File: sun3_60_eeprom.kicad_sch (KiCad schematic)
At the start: 19 parts, among them U2001 PAL16L8, U300 27512, U301 28C16, U302 7170, U303 32768Hz, U304 ALS273, U305 ALS373, U307 PAL20L8, U309 3-VOLT, U310 PAL20L8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

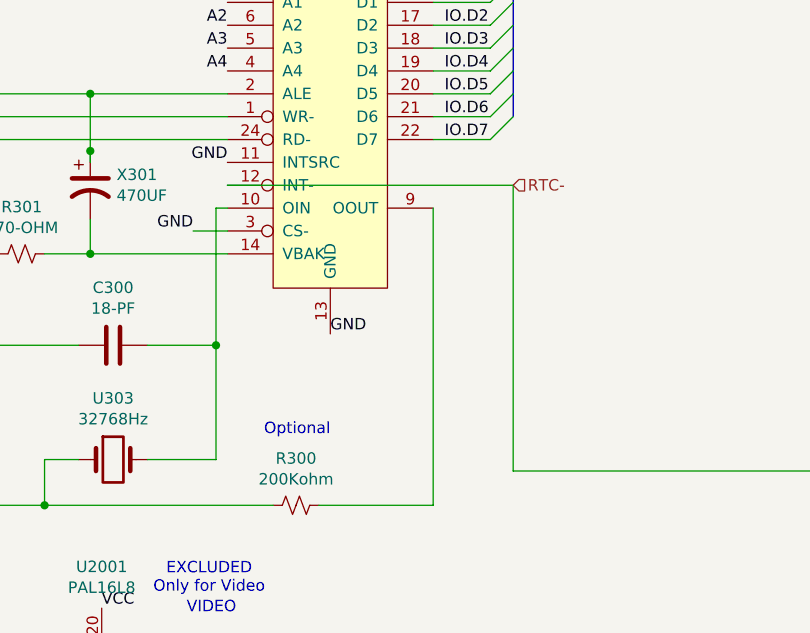
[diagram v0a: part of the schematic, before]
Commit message: Clean up before reorganizing the folders. The schematics and PCB reflect the fixes discovered during the prototype build.
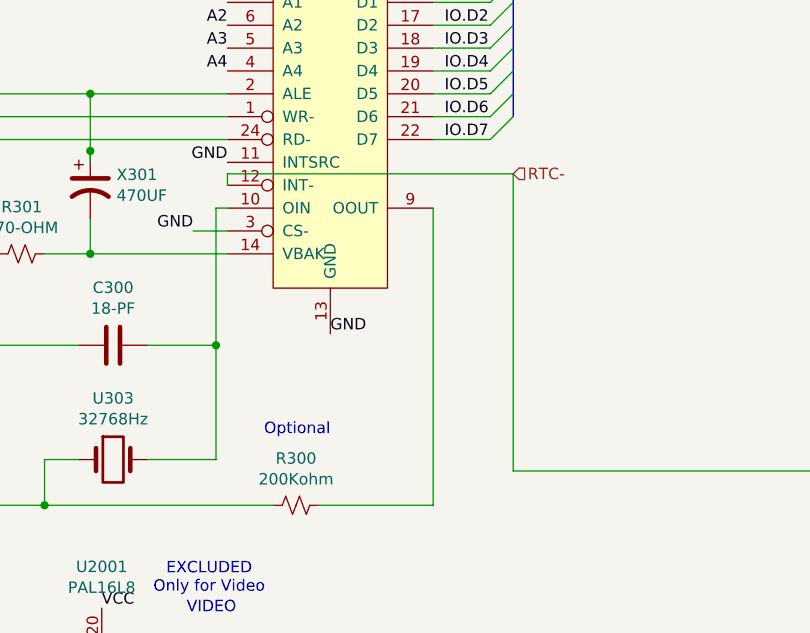
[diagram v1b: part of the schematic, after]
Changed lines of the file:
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@@
+	(wire
+		(pts
+			(xy 163.83 119.38) (xy 163.83 120.65)
+		)
+		(stroke
+			(width 0)
+			(type default)
+		)
+	)
 	(wire
 		(pts
@@
 	(wire
 		(pts
-			(xy 163.83 120.65) (xy 195.58 120.65)
+			(xy 163.83 119.38) (xy 195.58 119.38)
 		)
 		(stroke
@@
 	(wire
 		(pts
-			(xy 195.58 120.65) (xy 195.58 152.4)
+			(xy 195.58 119.38) (xy 195.58 152.4)
 		)
 		(stroke
@@
 	(hierarchical_label "RTC-"
 		(shape input)
-		(at 195.58 120.65 0)
-		(effects
-			(font
+		(at 195.58 119.38 0)
+		(effects
+			(font
